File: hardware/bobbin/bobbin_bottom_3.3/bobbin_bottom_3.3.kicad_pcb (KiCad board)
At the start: 2 copper layers, 68.5 x 8.5 mm, 5 parts, among them J1 OC, J2 OC, J3 IC, J4 IC

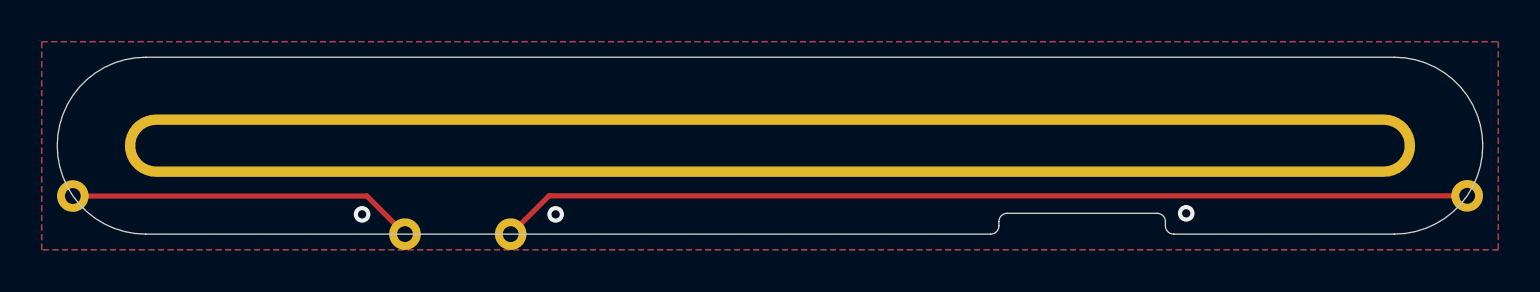
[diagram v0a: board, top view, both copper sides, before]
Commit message: adjusted for proper mouse-bites in panels
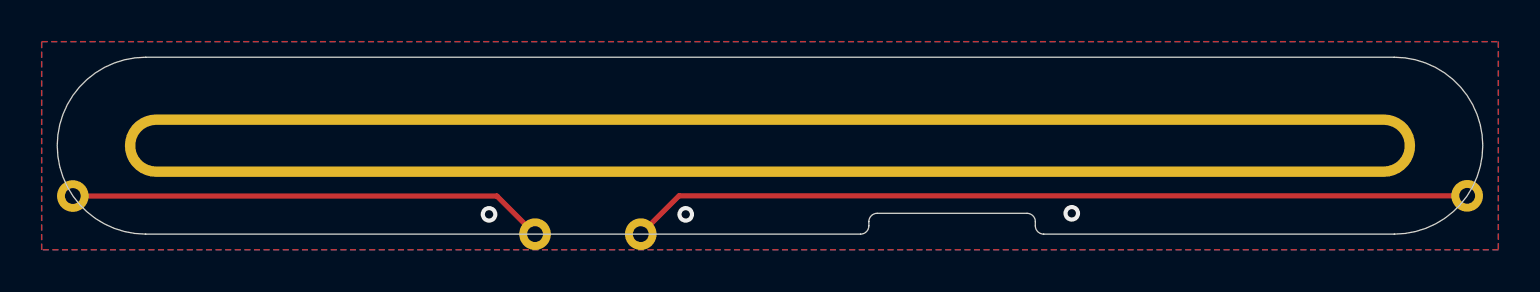
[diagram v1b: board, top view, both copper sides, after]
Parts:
- moved J1 6.25 mm to (123.8, 105.2)
- moved J4 6.25 mm to (118.7, 105.2)
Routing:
- net /OC: track 46.7 -> 40.5 mm
- net /IC: track 16.7 -> 23.0 mm
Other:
- outline, holes or cut-outs redrawn
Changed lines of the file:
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@@
   (net 3 "/IC")
   (footprint "cycfi_library:single-pad-1.52x1.52-th" (layer "F.Cu")
-    (at 117.54 105.25 180)
+    (at 123.79 105.25 180)
     (property "Sheetfile" "bobbin_bottom_3.3.kicad_sch")
     (property "Sheetname" "")
     (attr through_hole)
-    (fp_text reference "J1" (at 0 2.54 180) (layer "F.SilkS") hide
+    (fp_text reference "J1" (at 0 2.54) (layer "F.SilkS") hide
       (effects (font (size 1 1) (thickness 0.15)))
     )
-    (fp_text value "OC" (at 0 -2.54 180) (layer "F.Fab")
+    (fp_text value "OC" (at 0 -2.54) (layer "F.Fab")
       (effects (font (size 1 1) (thickness 0.15)))
     )
@@
   )
   (footprint "cycfi_library:single-pad-1.52x1.52-th" (layer "F.Cu")
-    (at 112.46 105.25)
+    (at 118.71 105.25)
     (property "Sheetfile" "bobbin_bottom_3.3.kicad_sch")
     (property "Sheetname" "")
@@
       (net 3 "/IC") (pinfunction "Pin_1") (pintype "passive"))
   )
-  (gr_arc (start 149.4 105.25) (mid 149.117157 105.132843) (end 149 104.85) (layer "Dwgs.User") (width 0.01))
+  (gr_arc (start 143.15 105.25) (mid 142.867157 105.132843) (end 142.75 104.85) (layer "Dwgs.User") (width 0.01))
   (gr_arc (start 160 96.75) (mid 164.25 101) (end 160 105.25) (layer "Dwgs.User") (width 0.01))
   (gr_line (start 100 100) (end 100 102) (layer "Dwgs.User") (width 0.01))
   (gr_line (start 100 96.75) (end 160 96.75) (layer "Dwgs.User") (width 0.01))
   (gr_line (start 100 102) (end 160 102) (layer "Dwgs.User") (width 0.01))
-  (gr_arc (start 141 104.65) (mid 141.117157 104.367157) (end 141.4 104.25) (layer "Dwgs.User") (width 0.01))
-  (gr_arc (start 148.6 104.25) (mid 148.882843 104.367157) (end 149 104.65) (layer "Dwgs.User") (width 0.01))
-  (gr_arc (start 111.698 105.25) (mid 112.46 104.488) (end 113.222 105.25) (layer "Dwgs.User") (width 0.01))
-  (gr_line (start 149 104.65) (end 149 104.85) (layer "Dwgs.User") (width 0.01))
-  (gr_arc (start 116.778 105.25) (mid 117.54 104.488) (end 118.302 105.25) (layer "Dwgs.User") (width 0.01))
-  (gr_line (start 160 105.25) (end 149.4 105.25) (layer "Dwgs.User") (width 0.01))
-  (gr_line (start 141 104.85) (end 141 104.65) (layer "Dwgs.User") (width 0.01))
+  (gr_arc (start 134.75 104.65) (mid 134.867157 104.367157) (end 135.15 104.25) (layer "Dwgs.User") (width 0.01))
+  (gr_arc (start 142.35 104.25) (mid 142.632843 104.367157) (end 142.75 104.65) (layer "Dwgs.User") (width 0.01))
+  (gr_arc (start 117.948 105.25) (mid 118.71 104.488) (end 119.472 105.25) (layer "Dwgs.User") (width 0.01))
+  (gr_line (start 142.75 104.65) (end 142.75 104.85) (layer "Dwgs.User") (width 0.01))
+  (gr_arc (start 123.028 105.25) (mid 123.79 104.488) (end 124.552 105.25) (layer "Dwgs.User") (width 0.01))
+  (gr_line (start 160 105.25) (end 143.15 105.25) (layer "Dwgs.User") (width 0.01))
+  (gr_line (start 134.75 104.85) (end 134.75 104.65) (layer "Dwgs.User") (width 0.01))
   (gr_line (start 160 100) (end 160 102) (layer "Dwgs.User") (width 0.01))
   (gr_arc (start 96.125734 102.747159) (mid 97.12753 102.978649) (end 96.986778 103.997164) (layer "Dwgs.User") (width 0.01))
   (gr_line (start 100 100) (end 160 100) (layer "Dwgs.User") (width 0.01))
-  (gr_arc (start 141 104.85) (mid 140.882843 105.132843) (end 140.6 105.25) (layer "Dwgs.User") (width 0.01))
-  (gr_line (start 140.6 105.25) (end 100 105.25) (layer "Dwgs.User") (width 0.01))
+  (gr_arc (start 134.75 104.85) (mid 134.632843 105.132843) (end 134.35 105.25) (layer "Dwgs.User") (width 0.01))
+  (gr_line (start 134.35 105.25) (end 100 105.25) (layer "Dwgs.User") (width 0.01))
   (gr_arc (start 163.013222 103.997164) (mid 162.872472 102.97865) (end 163.874266 102.747159) (layer "Dwgs.User") (width 0.01))
   (gr_arc (start 100 105.25) (mid 95.75 101) (end 100 96.75) (layer "Dwgs.User") (width 0.01))
-  (gr_line (start 141.4 104.25) (end 148.6 104.25) (layer "Dwgs.User") (width 0.01))
-  (gr_arc (start 148.6 104.25) (mid 148.882843 104.367157) (end 149 104.65) (layer "Edge.Cuts") (width 0.01))
-  (gr_line (start 141 104.85) (end 141 104.65) (layer "Edge.Cuts") (width 0.01))
-  (gr_line (start 149 104.65) (end 149 104.85) (layer "Edge.Cuts") (width 0.01))
-  (gr_arc (start 141 104.85) (mid 140.882843 105.132843) (end 140.6 105.25) (layer "Edge.Cuts") (width 0.01))
-  (gr_arc (start 141 104.65) (mid 141.117157 104.367157) (end 141.4 104.25) (layer "Edge.Cuts") (width 0.01))
+  (gr_line (start 135.15 104.25) (end 142.35 104.25) (layer "Dwgs.User") (width 0.01))
+  (gr_arc (start 142.35 104.25) (mid 142.632843 104.367157) (end 142.75 104.65) (layer "Edge.Cuts") (width 0.01))
+  (gr_line (start 134.75 104.85) (end 134.75 104.65) (layer "Edge.Cuts") (width 0.01))
+  (gr_line (start 142.75 104.65) (end 142.75 104.85) (layer "Edge.Cuts") (width 0.01))
+  (gr_arc (start 134.75 104.85) (mid 134.632843 105.132843) (end 134.35 105.25) (layer "Edge.Cuts") (width 0.01))
+  (gr_arc (start 134.75 104.65) (mid 134.867157 104.367157) (end 135.15 104.25) (layer "Edge.Cuts") (width 0.01))
   (gr_line (start 100 96.75) (end 160 96.75) (layer "Edge.Cuts") (width 0.01))
   (gr_arc (start 100 105.25) (mid 95.75 101) (end 100 96.75) (layer "Edge.Cuts") (width 0.01))
-  (gr_line (start 141.4 104.25) (end 148.6 104.25) (layer "Edge.Cuts") (width 0.01))
-  (gr_arc (start 149.4 105.25) (mid 149.117157 105.132843) (end 149 104.85) (layer "Edge.Cuts") (width 0.01))
-  (gr_line (start 140.6 105.25) (end 100 105.25) (layer "Edge.Cuts") (width 0.01))
-  (gr_line (start 160 105.25) (end 149.4 105.25) (layer "Edge.Cuts") (width 0.01))
+  (gr_line (start 135.15 104.25) (end 142.35 104.25) (layer "Edge.Cuts") (width 0.01))
+  (gr_arc (start 143.15 105.25) (mid 142.867157 105.132843) (end 142.75 104.85) (layer "Edge.Cuts") (width 0.01))
+  (gr_line (start 134.35 105.25) (end 100 105.25) (layer "Edge.Cuts") (width 0.01))
+  (gr_line (start 160 105.25) (end 143.15 105.25) (layer "Edge.Cuts") (width 0.01))
   (gr_arc (start 160 96.75) (mid 164.25 101) (end 160 105.25) (layer "Edge.Cuts") (width 0.01))
-  (via (at 110.4 104.3) (size 0.8) (drill 0.4) (layers "F.Cu" "B.Cu") (free) (net 1))
-  (via (at 150 104.25) (size 0.8) (drill 0.4) (layers "F.Cu" "B.Cu") (free) (net 1))
-  (via (at 119.7 104.3) (size 0.8) (drill 0.4) (layers "F.Cu" "B.Cu") (free) (net 1))
-  (segment (start 119.38 103.41) (end 117.54 105.25) (width 0.25) (layer "F.Cu") (net 2))
-  (segment (start 163.5 103.41) (end 119.38 103.41) (width 0.25) (layer "F.Cu") (net 2))
-  (segment (start 96.5 103.42) (end 110.63 103.42) (width 0.25) (layer "F.Cu") (net 3))
-  (segment (start 110.63 103.42) (end 112.46 105.25) (width 0.25) (layer "F.Cu") (net 3))
+  (via (at 116.5 104.3) (size 0.8) (drill 0.4) (layers "F.Cu" "B.Cu") (free) (net 1))
+  (via (at 144.5 104.25) (size 0.8) (drill 0.4) (layers "F.Cu" "B.Cu") (free) (net 1))
+  (via (at 125.95 104.3) (size 0.8) (drill 0.4) (layers "F.Cu" "B.Cu") (free) (net 1))
+  (segment (start 125.63 103.41) (end 123.79 105.25) (width 0.25) (layer "F.Cu") (net 2))
+  (segment (start 163.5 103.41) (end 125.63 103.41) (width 0.25) (layer "F.Cu") (net 2))
+  (segment (start 116.88 103.42) (end 118.71 105.25) (width 0.25) (layer "F.Cu") (net 3))
+  (segment (start 96.5 103.42) (end 116.88 103.42) (width 0.25) (layer "F.Cu") (net 3))
   (zone (net 1) (net_name "GND") (layer "F.Cu") (hatch edge 0.508)
     (connect_pads (clearance 0.25))
